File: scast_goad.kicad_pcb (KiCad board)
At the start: 2 copper layers, 91 x 80 mm, 11 parts, among them J1 Rotary Encoder, J2 Tilt_Sensor, SW5 SW_Push, SW6 SW_Push

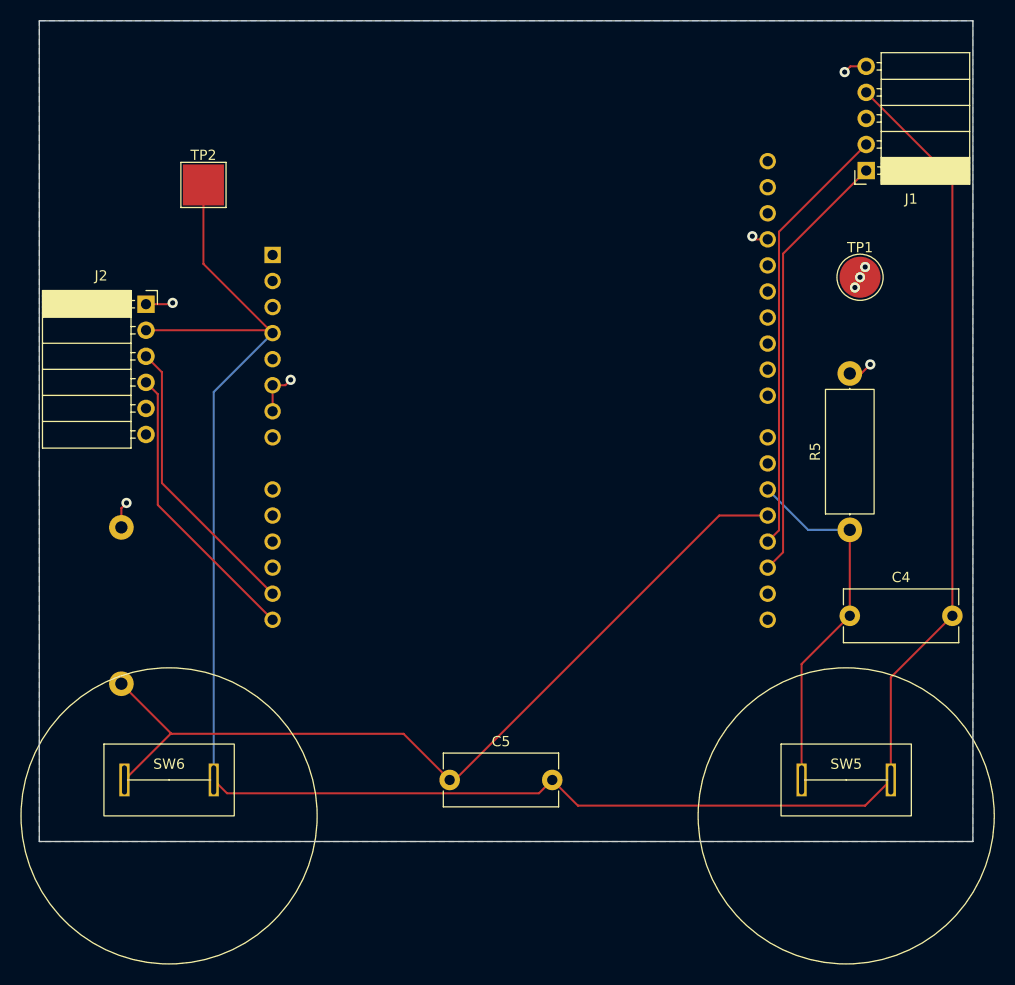
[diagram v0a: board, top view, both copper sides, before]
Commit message: Made track widths thicker
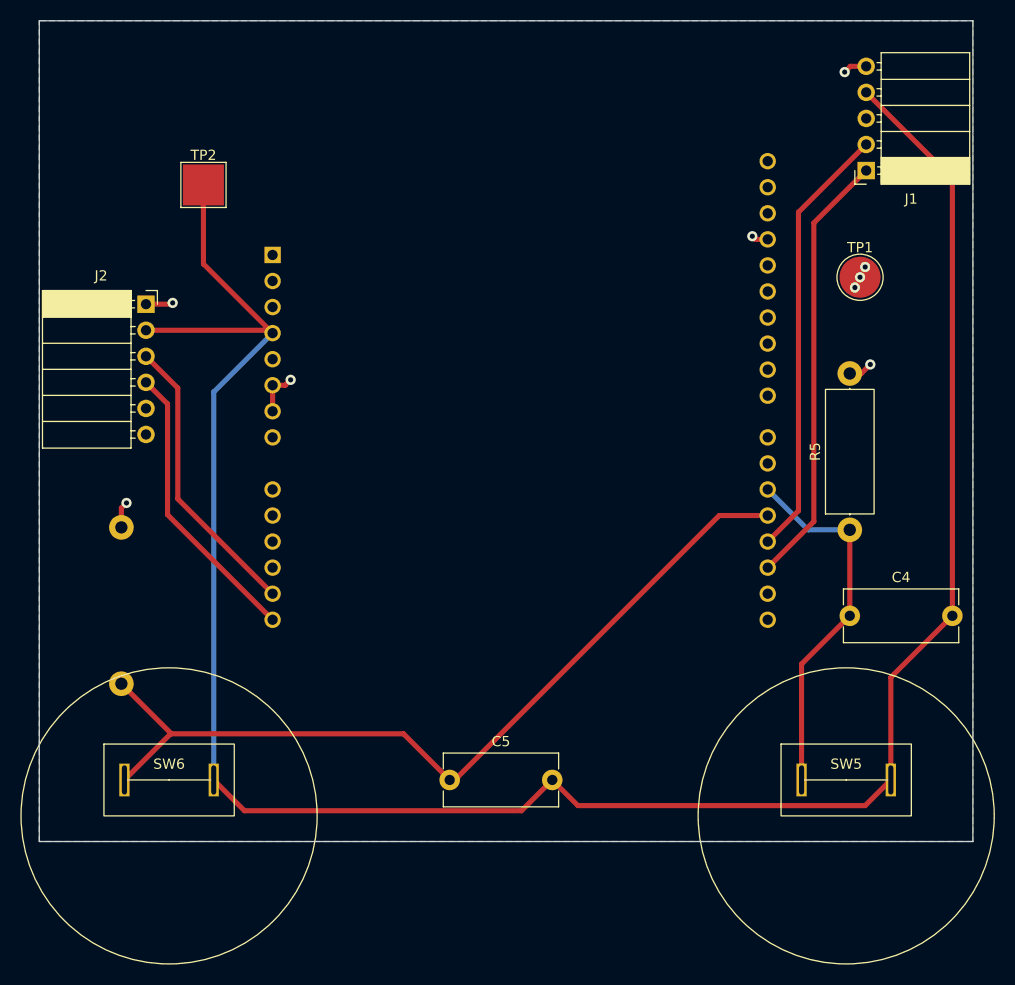
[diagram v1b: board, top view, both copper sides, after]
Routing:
- net +3V3: track 217.8 -> 219.2 mm
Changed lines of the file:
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@@
 		(capping no)
 		(filling no)
+		(zone_defaults)
 		(pcbplotparams
 			(layerselection 0x00000000_00000000_55555555_5755f5ff)
@@
 		(start 63.5 100)
 		(end 64 100)
-		(width 0.2)
+		(width 0.5)
 		(layer "F.Cu")
 		(net "BWD_SW")
@@
 		(start 36.38 95.5)
 		(end 36.3 95.5)
-		(width 0.2)
+		(width 0.5)
 		(layer "F.Cu")
 		(net "BWD_SW")
@@
 		(start 31.5 90.62)
 		(end 36.38 95.5)
-		(width 0.2)
+		(width 0.5)
 		(layer "F.Cu")
 		(net "BWD_SW")
@@
 		(start 63.5 100)
 		(end 59 95.5)
-		(width 0.2)
+		(width 0.5)
 		(layer "F.Cu")
 		(net "BWD_SW")
@@
 		(start 64 100)
 		(end 89.775 74.225)
-		(width 0.2)
+		(width 0.5)
 		(layer "F.Cu")
 		(net "BWD_SW")
@@
 		(start 36.3 95.5)
 		(end 31.8 100)
-		(width 0.2)
+		(width 0.5)
 		(layer "F.Cu")
 		(net "BWD_SW")
@@
 		(start 59 95.5)
 		(end 36.38 95.5)
-		(width 0.2)
+		(width 0.5)
 		(layer "F.Cu")
 		(net "BWD_SW")
@@
 		(start 89.775 74.225)
 		(end 94.5 74.225)
-		(width 0.2)
+		(width 0.5)
 		(layer "F.Cu")
 		(net "BWD_SW")
@@
 		(start 33.9 56.165)
 		(end 45.96 56.165)
-		(width 0.2)
+		(width 0.5)
 		(layer "F.Cu")
 		(net "+3V3")
@@
 		(start 45.96 56.165)
 		(end 46.24 56.445)
-		(width 0.2)
+		(width 0.5)
 		(layer "F.Cu")
 		(net "+3V3")
 	)
 	(segment
-		(start 72.2 101.3)
-		(end 73.5 100)
-		(width 0.2)
+		(start 40.5 100)
+		(end 43.5 103)
+		(width 0.5)
+		(layer "F.Cu")
+		(net "+3V3")
+	)
+	(segment
+		(start 43.5 103)
+		(end 70.5 103)
+		(width 0.5)
 		(layer "F.Cu")
 		(net "+3V3")
@@
 		(start 106.5 90)
 		(end 112.5 84)
-		(width 0.2)
+		(width 0.5)
 		(layer "F.Cu")
 		(net "+3V3")
@@
 		(start 73.5 100)
 		(end 76 102.5)
-		(width 0.2)
+		(width 0.5)
 		(layer "F.Cu")
 		(net "+3V3")
@@
 		(start 112.5 41.38)
 		(end 112.5 84)
-		(width 0.2)
+		(width 0.5)
 		(layer "F.Cu")
 		(net "+3V3")
@@
 		(start 46.24 56.445)
 		(end 39.5 49.705)
-		(width 0.2)
+		(width 0.5)
 		(layer "F.Cu")
 		(net "+3V3")
@@
 		(start 106.5 100)
 		(end 106.5 90)
-		(width 0.2)
+		(width 0.5)
 		(layer "F.Cu")
 		(net "+3V3")
@@
 		(start 76 102.5)
 		(end 104 102.5)
-		(width 0.2)
+		(width 0.5)
 		(layer "F.Cu")
 		(net "+3V3")
 	)
 	(segment
-		(start 104.1 32.98)
-		(end 112.5 41.38)
-		(width 0.2)
+		(start 70.5 103)
+		(end 73.5 100)
+		(width 0.5)
 		(layer "F.Cu")
 		(net "+3V3")
 	)
 	(segment
-		(start 41.8 101.3)
-		(end 72.2 101.3)
-		(width 0.2)
+		(start 104.1 32.98)
+		(end 112.5 41.38)
+		(width 0.5)
 		(layer "F.Cu")
 		(net "+3V3")
@@
 		(start 39.5 49.705)
 		(end 39.5 42)
-		(width 0.2)
+		(width 0.5)
 		(layer "F.Cu")
 		(net "+3V3")
@@
 		(start 104 102.5)
 		(end 106.5 100)
-		(width 0.2)
-		(layer "F.Cu")
-		(net "+3V3")
-	)
-	(segment
-		(start 40.5 100)
-		(end 41.8 101.3)
-		(width 0.2)
+		(width 0.5)
 		(layer "F.Cu")
 		(net "+3V3")
@@
 		(start 40.5 100)
 		(end 40.5 62.185)
-		(width 0.2)
+		(width 0.5)
 		(layer "B.Cu")
 		(net "+3V3")
@@
 		(start 40.5 62.185)
 		(end 46.24 56.445)
-		(width 0.2)
+		(width 0.5)
 		(layer "B.Cu")
 		(net "+3V3")
@@
 		(start 102.5 84)
 		(end 102.5 75.62)
-		(width 0.2)
+		(width 0.5)
 		(layer "F.Cu")
 		(net "FWD_SW")
@@
 		(start 97.8 88.7)
 		(end 102.5 84)
-		(width 0.2)
+		(width 0.5)
 		(layer "F.Cu")
 		(net "FWD_SW")
@@
 		(start 97.8 100)
 		(end 97.8 88.7)
-		(width 0.2)
+		(width 0.5)
 		(layer "F.Cu")
 		(net "FWD_SW")
@@
 		(start 98.435 75.62)
 		(end 94.5 71.685)
-		(width 0.2)
+		(width 0.5)
 		(layer "B.Cu")
 		(net "FWD_SW")
@@
 		(start 102.5 75.62)
 		(end 98.435 75.62)
-		(width 0.2)
+		(width 0.5)
 		(layer "B.Cu")
 		(net "FWD_SW")
@@
 		(start 46.24 61.525)
 		(end 47.475 61.525)
-		(width 0.2)
+		(width 0.5)
 		(layer "F.Cu")
 		(net "GND")
@@
 		(start 93.305 47.305)
 		(end 93 47)
-		(width 0.2)
+		(width 0.5)
 		(layer "F.Cu")
 		(net "GND")
@@
 		(start 102 31)
 		(end 102.56 30.44)
-		(width 0.2)
+		(width 0.5)
 		(layer "F.Cu")
 		(net "GND")
@@
 		(start 47.475 61.525)
 		(end 48 61)
-		(width 0.2)
+		(width 0.5)
 		(layer "F.Cu")
 		(net "GND")
@@
 		(start 33.9 53.625)
 		(end 36.375 53.625)
-		(width 0.2)
+		(width 0.5)
 		(layer "F.Cu")
 		(net "GND")
@@
 		(start 103.62 60.38)
 		(end 104.5 59.5)
-		(width 0.2)
+		(width 0.5)
 		(layer "F.Cu")
 		(net "GND")
@@
 		(start 36.375 53.625)
 		(end 36.5 53.5)
-		(width 0.2)
+		(width 0.5)
 		(layer "F.Cu")
 		(net "GND")
@@
 		(start 94.5 47.305)
 		(end 93.305 47.305)
-		(width 0.2)
+		(width 0.5)
 		(layer "F.Cu")
 		(net "GND")
@@
 		(start 31.5 73.5)
 		(end 31.5 75.38)
-		(width 0.2)
+		(width 0.5)
 		(layer "F.Cu")
 		(net "GND")
@@
 		(start 102.56 30.44)
 		(end 104.1 30.44)
-		(width 0.2)
+		(width 0.5)
 		(layer "F.Cu")
 		(net "GND")
@@
 		(start 32 73)
 		(end 31.5 73.5)
-		(width 0.2)
+		(width 0.5)
 		(layer "F.Cu")
 		(net "GND")
@@
 		(start 102.5 60.38)
 		(end 103.62 60.38)
-		(width 0.2)
+		(width 0.5)
 		(layer "F.Cu")
 		(net "GND")
@@
 		(start 46.24 64.065)
 		(end 46.24 61.525)
-		(width 0.2)
+		(width 0.5)
 		(layer "F.Cu")
 		(net "GND")
@@
 	)
 	(segment
-		(start 96 48.7)
-		(end 104.1 40.6)
-		(width 0.2)
+		(start 99 74.805)
+		(end 99 45.7)
+		(width 0.5)
 		(layer "F.Cu")
 		(net "ENCODER_A")
@@
 	(segment
 		(start 94.5 79.305)
-		(end 96 77.805)
-		(width 0.2)
+		(end 99 74.805)
+		(width 0.5)
 		(layer "F.Cu")
 		(net "ENCODER_A")
 	)
 	(segment
-		(start 96 77.805)
-		(end 96 48.7)
-		(width 0.2)
+		(start 99 45.7)
+		(end 104.1 40.6)
+		(width 0.5)
 		(layer "F.Cu")
 		(net "ENCODER_A")
 	)
 	(segment
-		(start 94.5 76.765)
-		(end 95.6 75.665)
-		(width 0.2)
+		(start 97.5 44.66)
+		(end 104.1 38.06)
+		(width 0.5)
 		(layer "F.Cu")
 		(net "ENCODER_B")
 	)
 	(segment
-		(start 95.6 46.56)
-		(end 104.1 38.06)
-		(width 0.2)
+		(start 97.5 73.765)
+		(end 97.5 44.66)
+		(width 0.5)
 		(layer "F.Cu")
 		(net "ENCODER_B")
 	)
 	(segment
-		(start 95.6 75.665)
-		(end 95.6 46.56)
-		(width 0.2)
+		(start 94.5 76.765)
+		(end 97.5 73.765)
+		(width 0.5)
 		(layer "F.Cu")
 		(net "ENCODER_B")
 	)
 	(segment
-		(start 35.45 71.055)
+		(start 37 72.605)
 		(end 46.24 81.845)
-		(width 0.2)
+		(width 0.5)
 		(layer "F.Cu")
 		(net "TILT_SDA")
@@
 	(segment
 		(start 33.9 58.705)
-		(end 35.45 60.255)
-		(width 0.2)
+		(end 37 61.805)
+		(width 0.5)
 		(layer "F.Cu")
 		(net "TILT_SDA")
 	)
 	(segment
-		(start 35.45 60.255)
-		(end 35.45 71.055)
-		(width 0.2)
+		(start 37 61.805)
+		(end 37 72.605)
+		(width 0.5)
 		(layer "F.Cu")
 		(net "TILT_SDA")
 	)
 	(segment
-		(start 33.9 61.245)
-		(end 35.05 62.395)
-		(width 0.2)
+		(start 36 74.145)
+		(end 46.24 84.385)
+		(width 0.5)
 		(layer "F.Cu")
 		(net "TILT_SCL")
 	)
 	(segment
-		(start 35.05 73.195)
-		(end 46.24 84.385)
-		(width 0.2)
+		(start 33.9 61.245)
+		(end 36 63.345)
+		(width 0.5)
 		(layer "F.Cu")
 		(net "TILT_SCL")
 	)
 	(segment
-		(start 35.05 62.395)
-		(end 35.05 73.195)
-		(width 0.2)
+		(start 36 63.345)
+		(end 36 74.145)
+		(width 0.5)
 		(layer "F.Cu")
 		(net "TILT_SCL")
